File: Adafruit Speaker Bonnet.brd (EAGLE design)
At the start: 65 x 30 mm, 32 parts, among them X1 3.5mm, X2 3.5mm, X3 4 JST-PH

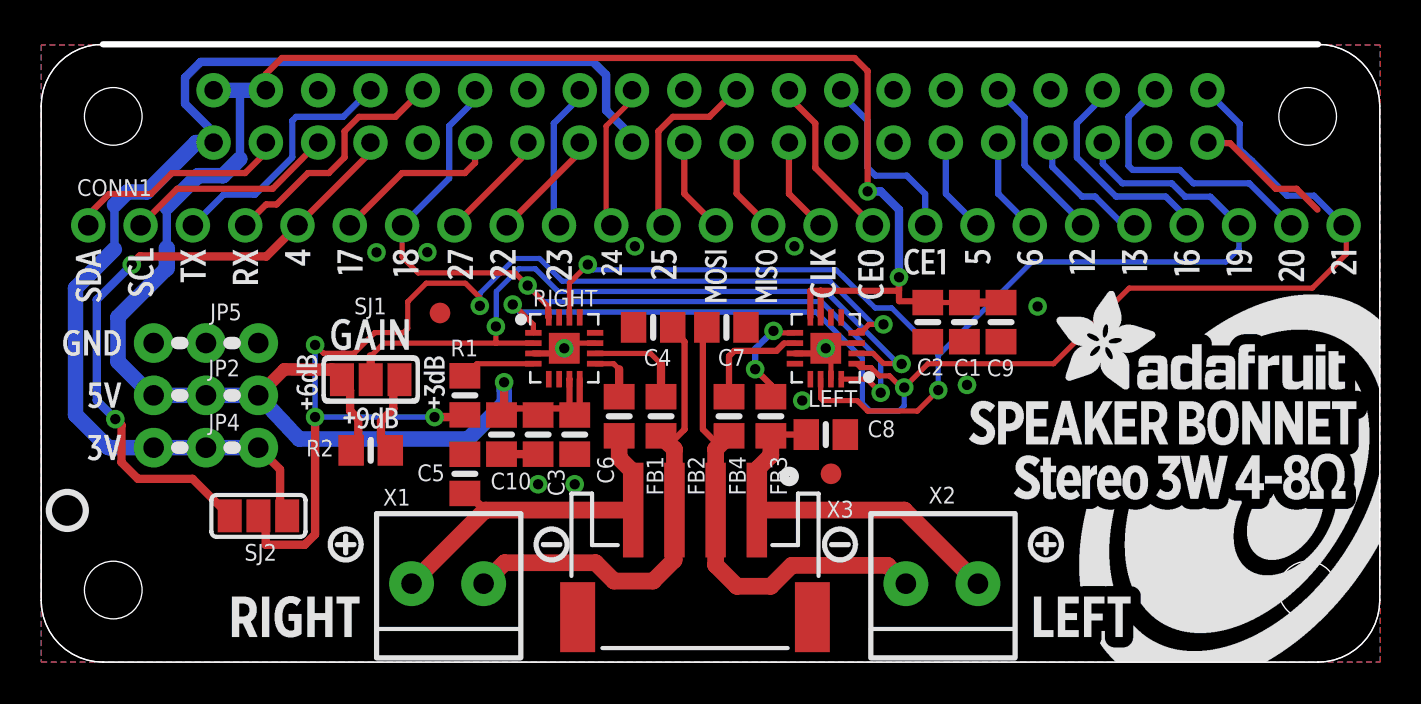
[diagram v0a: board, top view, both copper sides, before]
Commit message: swap LEFT-RIGHT
* swap channels (does not impact software side)
* upate silkscreen (now right-side output is actually RIGHT channel)
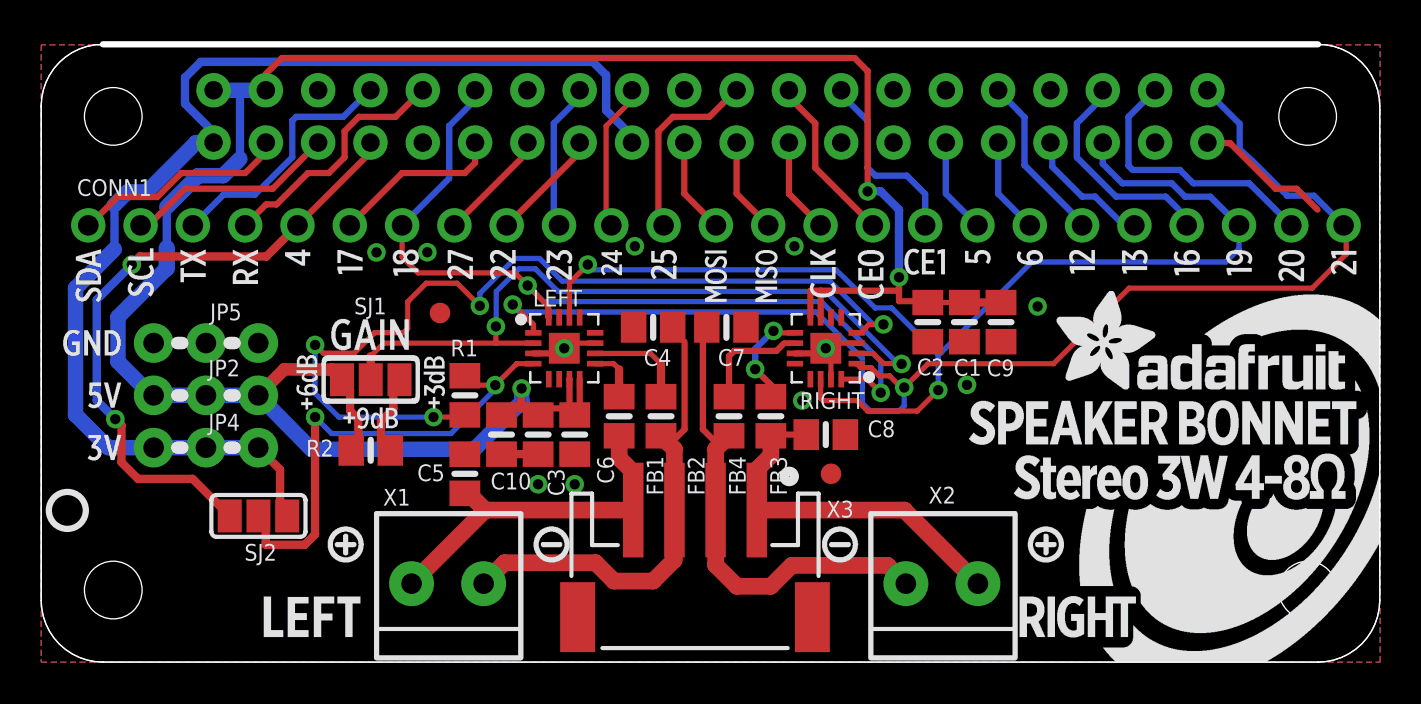
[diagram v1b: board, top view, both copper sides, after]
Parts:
- U$30: device microbuilder:BONNET_SPEAKER_REVB -> microbuilder:BONNET_SPEAKER_REVB_LR
- moved LEFT 12.7 mm to (25.4, 15.2), turned to 0 degrees
- moved RIGHT 12.7 mm to (38.1, 15.2), turned to 180 degrees
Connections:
- removed net SD_MODE: R1.1, RIGHT.4
- new net N$3: R1.2, RIGHT.4
- net !SD: now also R1.1; no longer R1.2
- net LEFT+: now also C5.1, FB1.2, X1.2, X3.4; no longer C8.1, FB3.2, X2.1, X3.1
- net LEFT-: now also C4.1, FB2.2, X1.1, X3.3; no longer C7.1, FB4.2, X2.2, X3.2
- net N$1: now also RIGHT.10; no longer LEFT.10
- net N$2: now also RIGHT.9; no longer LEFT.9
- net N$5: now also LEFT.10; no longer RIGHT.10
- net N$6: now also LEFT.9; no longer RIGHT.9
- net RIGHT+: now also C8.1, FB3.2, X2.1, X3.1; no longer C5.1, FB1.2, X1.2, X3.4
- net RIGHT-: now also C7.1, FB4.2, X2.2, X3.2; no longer C4.1, FB2.2, X1.1, X3.3
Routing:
- net N$3: track 0.00 -> 44.6 mm, vias 0 -> 4
- net !SD: track 55.9 -> 24.5 mm, vias 5 -> 2
- net SD_MODE: track 3.57 -> 0.00 mm
- net LEFT-: track 23.3 -> 22.1 mm
